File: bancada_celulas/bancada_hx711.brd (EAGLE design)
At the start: 124.4 x 102.5 mm, 17 parts

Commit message: KK connectors changed from 4mm to 2.54mm
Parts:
- X1, X11, X2, X3, X4, X5: value (none) -> 22-23-2041; device con-molex:KK-156-4 -> con-molex:22-23-2041
- X10, X6, X7, X8, X9: value (none) -> 22-23-2021; device con-molex:KK-156-2 -> con-molex:22-23-2021
- moved X10 6.35 mm to (91.4, 94.0)
- moved X9 5.08 mm to (67.3, 94.0)
- moved X8 5.08 mm to (19.1, 94.0)
- moved X6 5.08 mm to (115.6, 94.0)
- moved X4 3.81 mm to (88.9, 81.3)
- moved X5 2.54 mm to (113.0, 81.3)
- moved X1 2.54 mm to (16.5, 81.3)
- moved X3 2.54 mm to (64.8, 81.3)
- moved X7 2.54 mm to (43.2, 94.0)
- moved X2 1.27 mm to (40.6, 81.3)
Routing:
- net N$16: track 15.3 -> 12.7 mm
- net VCC: track 227.0 -> 229.1 mm
- net N$20: track 14.8 -> 12.7 mm
- net N$12: track 14.8 -> 12.7 mm
- net N$4: track 14.8 -> 12.7 mm
- net N$15: track 14.6 -> 12.7 mm
- net N$13: track 14.4 -> 12.7 mm
- net N$14: track 14.3 -> 12.7 mm
- net N$5: track 14.2 -> 12.7 mm
- net N$11: track 14.1 -> 12.7 mm
- net N$3: track 14.1 -> 12.7 mm
- net N$19: track 14.1 -> 12.7 mm
- net N$10: track 13.8 -> 12.7 mm
- net N$2: track 13.8 -> 12.7 mm
- net N$18: track 13.8 -> 12.7 mm
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
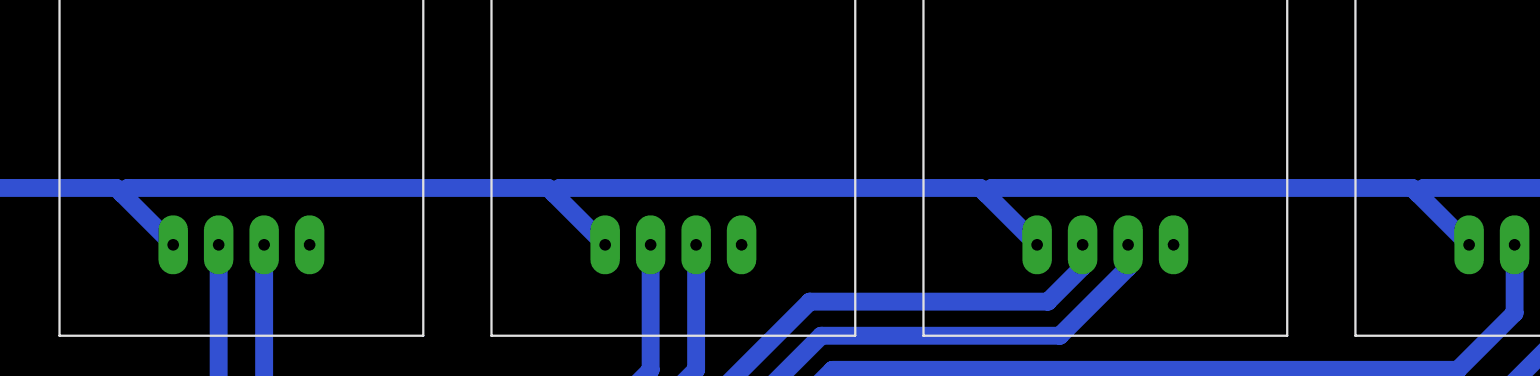
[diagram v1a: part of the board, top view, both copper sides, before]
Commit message: Increase the width of the grounded pins bridges and update DRC
The connections between the GND pins and the GND plane were too thin, so on the milling process they ended up not connected.

To solve this problem the width of those bridges were increased from 0.1016mm to 0.762mm changinf the GND polygon to 1.016mm width.

A new DRC was created as is used by both boards.
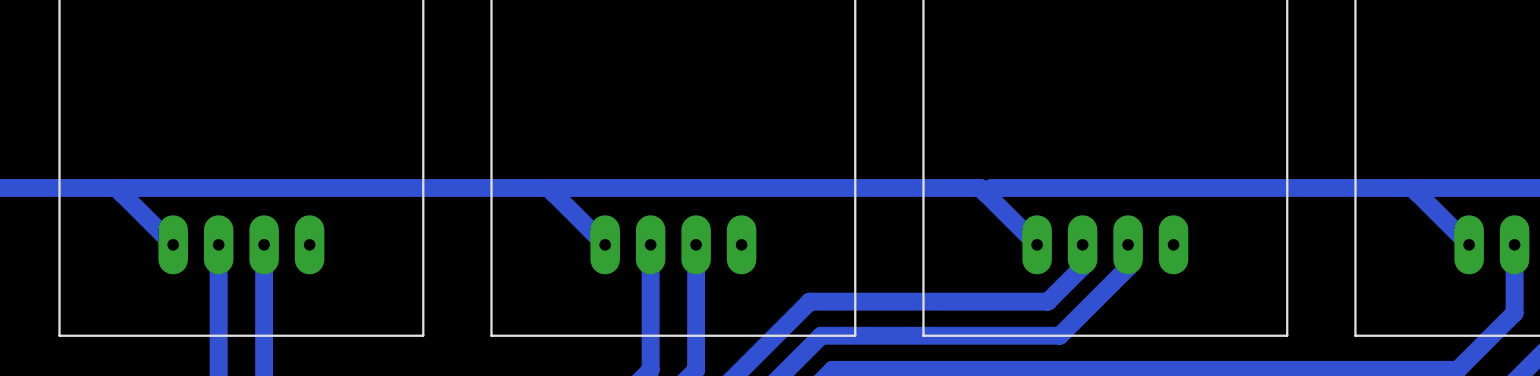
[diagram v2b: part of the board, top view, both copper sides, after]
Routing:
- net VCC: track 229.1 -> 231.0 mm
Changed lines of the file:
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@@
 <setting verticaltext="up"/>
 </settings>
-<grid distance="50" unitdist="mil" unit="mm" style="lines" multiple="1" display="no" altdistance="5" altunitdist="mil" altunit="mil"/>
+<grid distance="0.1" unitdist="mm" unit="mm" style="lines" multiple="1" display="no" altdistance="5" altunitdist="mil" altunit="mil"/>
 <layers>
 <layer number="1" name="Top" color="4" fill="1" visible="yes" active="yes"/>
@@
 </class>
 </classes>
-<designrules name="regraspcb2">
+<designrules name="drc_inep">
 <description language="de">&lt;b&gt;EAGLE Design Rules&lt;/b&gt;
 &lt;p&gt;
@@
 <param name="mtCopper" value="0.035mm 0.035mm 0.035mm 0.035mm 0.035mm 0.035mm 0.035mm 0.035mm 0.035mm 0.035mm 0.035mm 0.035mm 0.035mm 0.035mm 0.035mm 0.035mm"/>
 <param name="mtIsolate" value="1.5mm 0.15mm 0.2mm 0.15mm 0.2mm 0.15mm 0.2mm 0.15mm 0.2mm 0.15mm 0.2mm 0.15mm 0.2mm 0.15mm 0.2mm"/>
-<param name="mdWireWire" value="30mil"/>
-<param name="mdWirePad" value="30mil"/>
-<param name="mdWireVia" value="30mil"/>
-<param name="mdPadPad" value="30mil"/>
-<param name="mdPadVia" value="30mil"/>
-<param name="mdViaVia" value="30mil"/>
-<param name="mdSmdPad" value="30mil"/>
-<param name="mdSmdVia" value="30mil"/>
-<param name="mdSmdSmd" value="30mil"/>
+<param name="mdWireWire" value="20mil"/>
+<param name="mdWirePad" value="20mil"/>
+<param name="mdWireVia" value="20mil"/>
+<param name="mdPadPad" value="20mil"/>
+<param name="mdPadVia" value="20mil"/>
+<param name="mdViaVia" value="20mil"/>
+<param name="mdSmdPad" value="20mil"/>
+<param name="mdSmdVia" value="20mil"/>
+<param name="mdSmdSmd" value="20mil"/>
 <param name="mdViaViaSameLayer" value="8mil"/>
 <param name="mnLayersViaInSmd" value="2"/>
-<param name="mdCopperDimension" value="0.5mm"/>
+<param name="mdCopperDimension" value="1mm"/>
 <param name="mdDrill" value="1.5mm"/>
 <param name="mdSmdStop" value="0mil"/>
-<param name="msWidth" value="1mm"/>
-<param name="msDrill" value="1mm"/>
+<param name="msWidth" value="20mil"/>
+<param name="msDrill" value="0.2mm"/>
 <param name="msMicroVia" value="9.99mm"/>
 <param name="msBlindViaRatio" value="0.5"/>
@@
 <wire x1="103.505" y1="46.355" x2="103.8225" y2="46.0375" width="1" layer="16"/>
 <wire x1="103.8225" y1="46.0375" x2="106.68" y2="43.18" width="1" layer="16"/>
-<wire x1="80.01" y1="46.355" x2="103.505" y2="46.355" width="1" layer="16"/>
+<wire x1="80.01" y1="46.355" x2="102.87" y2="46.355" width="1" layer="16"/>
+<wire x1="102.87" y1="46.355" x2="103.505" y2="46.355" width="1" layer="16"/>
 <wire x1="80.01" y1="46.355" x2="79.6925" y2="46.0375" width="1" layer="16"/>
 <wire x1="29.845" y1="20.955" x2="62.23" y2="20.955" width="1" layer="16"/>
@@
 <wire x1="10.16" y1="45.085" x2="10.16" y2="43.18" width="1" layer="16"/>
 <wire x1="106.68" y1="26.67" x2="106.68" y2="24.13" width="1" layer="16"/>
+<wire x1="31.75" y1="46.355" x2="31.115" y2="46.355" width="1" layer="16"/>
+<wire x1="55.88" y1="46.355" x2="55.245" y2="46.355" width="1" layer="16"/>
+<wire x1="104.14" y1="46.355" x2="103.505" y2="46.355" width="1" layer="16"/>
 </signal>
 <signal name="GND">
@@
 <contactref element="X10" pad="2"/>
 <contactref element="X11" pad="3"/>
-<polygon width="0.1524" layer="16">
+<polygon width="0.762" layer="16">
 <vertex x="-5.08" y="106.68"/>
 <vertex x="128.27" y="106.68"/>

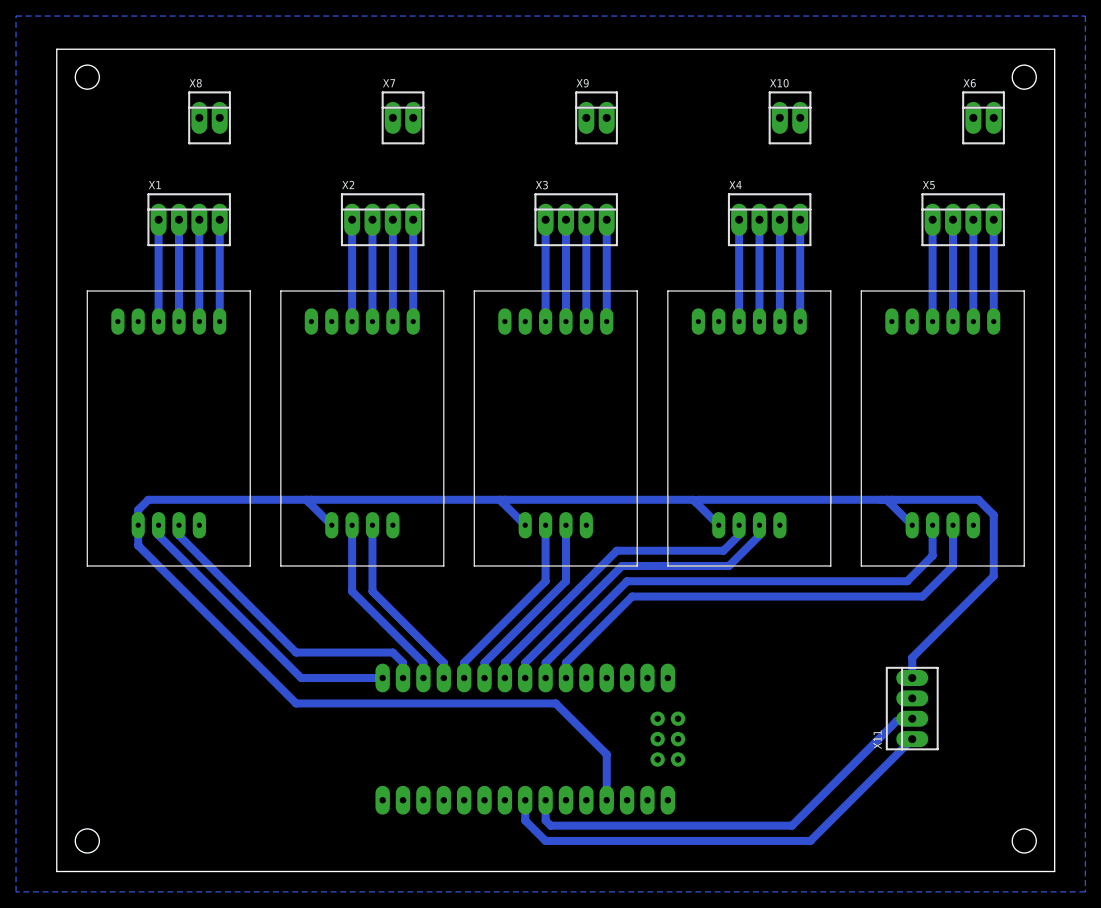
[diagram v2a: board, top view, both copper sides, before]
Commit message: Correct position for edge lines
Both top and right edge lines were bad positioned, in a way that the four board holes were not the same distance from the edges. This makes dificult to position them on CAD files for posterior case modeling.

Now the holes are 150mil apart from each edge.
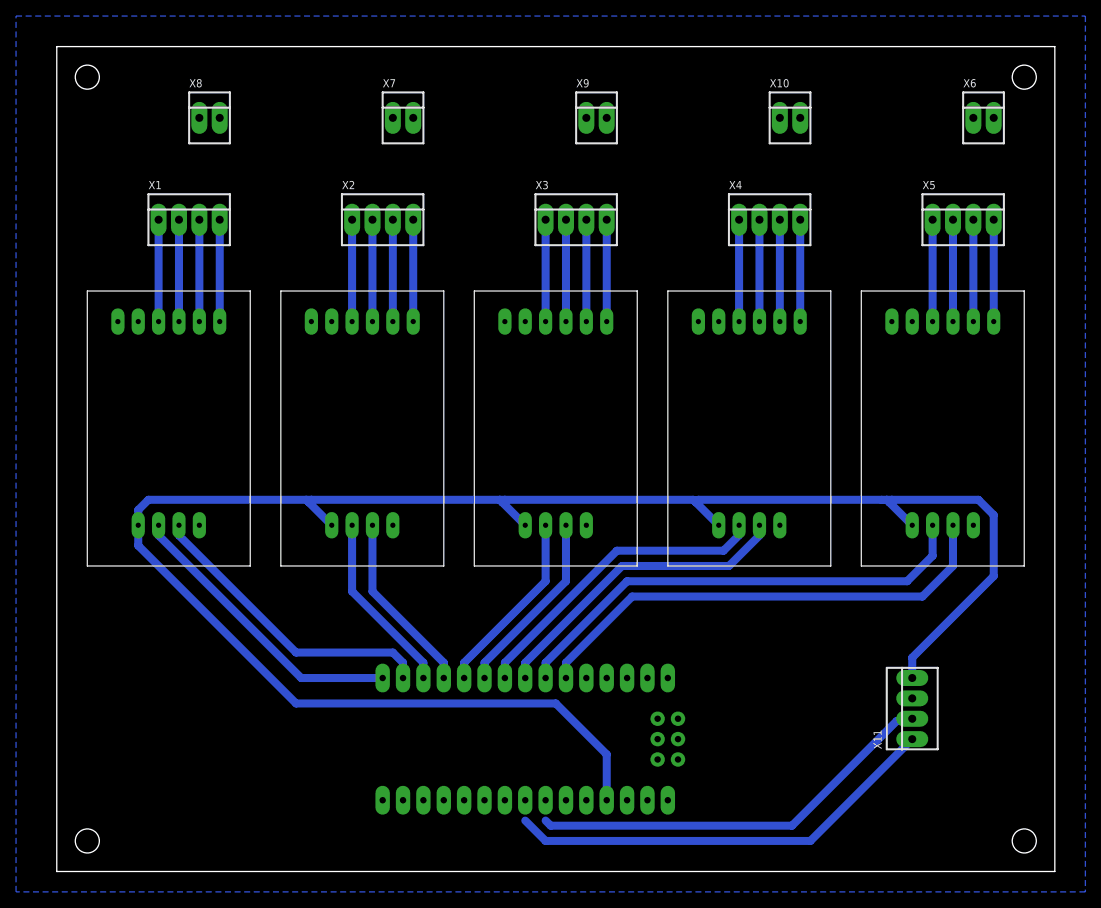
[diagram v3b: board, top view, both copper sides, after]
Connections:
- net N$21 renamed A5
- net N$22 renamed A4
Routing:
- net A4: track 57.1 -> 54.6 mm
- net A5: track 54.0 -> 51.5 mm
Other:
- board size 124.4 x 102.5 mm -> 124.5 x 102.9 mm
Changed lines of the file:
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@@
 <?xml version="1.0" encoding="utf-8"?>
 <!DOCTYPE eagle SYSTEM "eagle.dtd">
-<eagle version="8.6.0">
+<eagle version="9.0.0">
 <drawing>
 <settings>
@@
 <setting verticaltext="up"/>
 </settings>
-<grid distance="0.1" unitdist="mm" unit="mm" style="lines" multiple="1" display="no" altdistance="5" altunitdist="mil" altunit="mil"/>
+<grid distance="3.93700787" unitdist="mil" unit="inch" style="lines" multiple="1" display="no" altdistance="5" altunitdist="mil" altunit="mil"/>
 <layers>
 <layer number="1" name="Top" color="4" fill="1" visible="yes" active="yes"/>
@@
 <board>
 <plain>
-<wire x1="0" y1="0" x2="124.44" y2="0" width="0" layer="20"/>
-<wire x1="124.44" y1="0" x2="124.44" y2="102.54" width="0" layer="20"/>
-<wire x1="124.44" y1="102.54" x2="0" y2="102.54" width="0" layer="20"/>
-<wire x1="0" y1="102.54" x2="0" y2="0" width="0" layer="20"/>
+<wire x1="0" y1="0" x2="124.46" y2="0" width="0" layer="20"/>
+<wire x1="124.46" y1="0" x2="124.46" y2="102.87" width="0" layer="20"/>
+<wire x1="124.46" y1="102.87" x2="0" y2="102.87" width="0" layer="20"/>
+<wire x1="0" y1="102.87" x2="0" y2="0" width="0" layer="20"/>
 <hole x="3.81" y="3.81" drill="3"/>
 <hole x="120.65" y="3.81" drill="3"/>
@@
 <wire x1="109.22" y1="81.28" x2="109.22" y2="68.58" width="1" layer="16"/>
 </signal>
-<signal name="N$21">
+<signal name="A5">
 <contactref element="U$1" pad="A5"/>
 <contactref element="X11" pad="2"/>
-<wire x1="60.96" y1="8.89" x2="60.96" y2="6.35" width="1" layer="16"/>
 <wire x1="61.595" y1="5.715" x2="60.96" y2="6.35" width="1" layer="16"/>
 <wire x1="106.68" y1="19.05" x2="106.402" y2="18.772" width="1" layer="16"/>
@@
 <wire x1="104.74304375" y1="18.772" x2="91.68604375" y2="5.715" width="1" layer="16"/>
 <wire x1="91.68604375" y1="5.715" x2="61.595" y2="5.715" width="1" layer="16"/>
-</signal>
-<signal name="N$22">
+<wire x1="60.96" y1="6.35" x2="60.96" y2="8.89" width="0" layer="19" extent="16-16"/>
+</signal>
+<signal name="A4">
 <contactref element="U$1" pad="A4"/>
 <contactref element="X11" pad="1"/>
-<wire x1="58.42" y1="8.89" x2="58.42" y2="6.35" width="1" layer="16"/>
 <wire x1="60.96" y1="3.81" x2="58.42" y2="6.35" width="1" layer="16"/>
 <wire x1="106.68" y1="16.51" x2="93.98" y2="3.81" width="1" layer="16"/>
 <wire x1="93.98" y1="3.81" x2="60.96" y2="3.81" width="1" layer="16"/>
+<wire x1="58.42" y1="6.35" x2="58.42" y2="8.89" width="0" layer="19" extent="16-16"/>
 </signal>
 </signals>

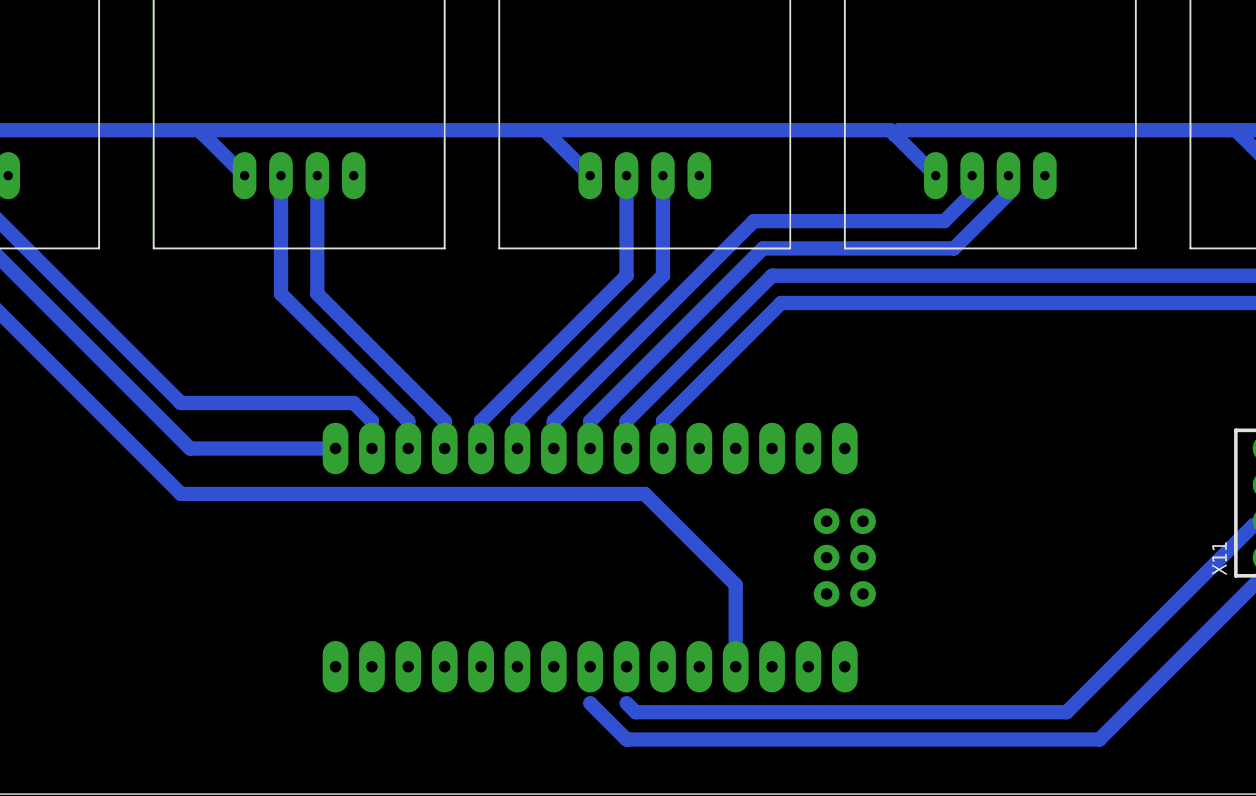
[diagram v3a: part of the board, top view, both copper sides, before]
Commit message: Add jumpers (or 0ohm resistors)
In previous design, some ground planes were unconnected to each other. It was meant to be added jumper wires after production.

This commit changes this to actual jumpers, with pins, so they don't need to be soldered from bottom, but can actually be placed on top, like any other through-hole component. 0ohm through-hole resistors can also be used.
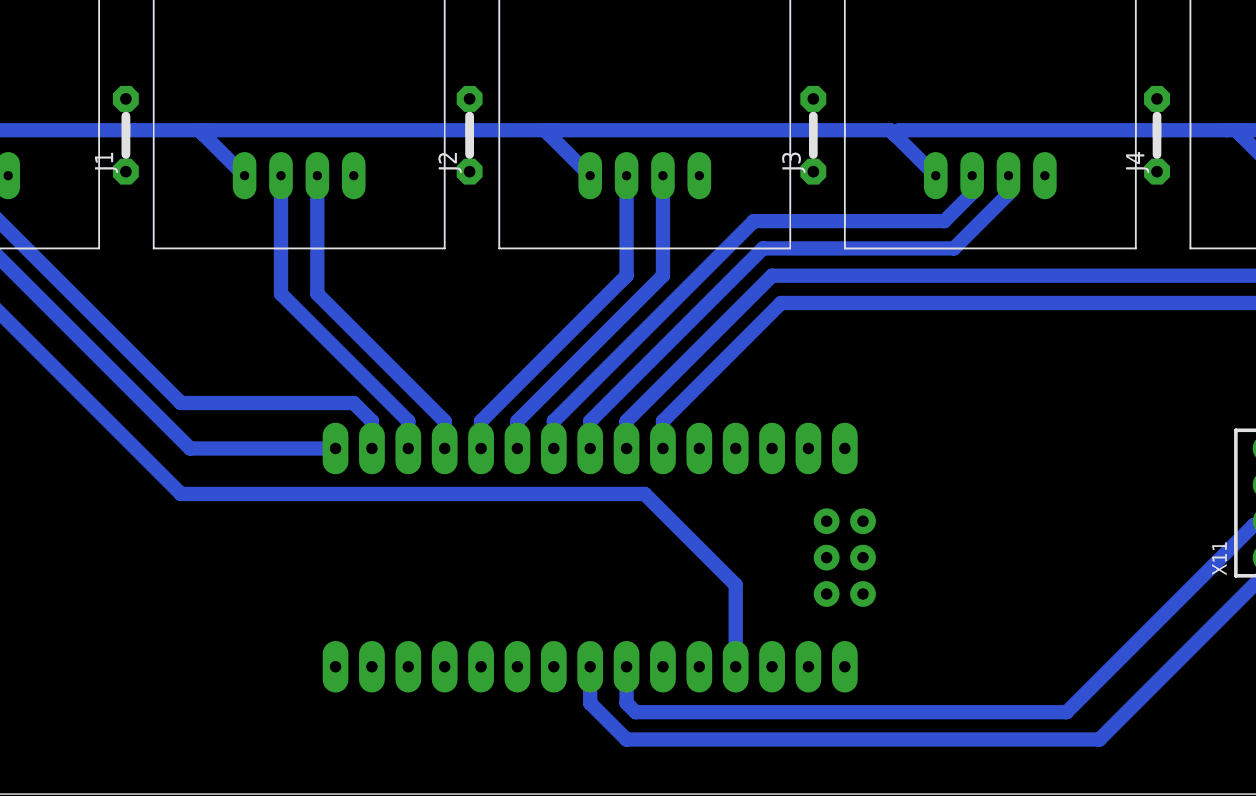
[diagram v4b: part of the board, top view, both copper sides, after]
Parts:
- added J1, J2, J3, J4: J5MM, jumper:05
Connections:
- net GND: now also J1.1, J1.2, J2.1, J2.2, J3.1, J3.2, J4.1, J4.2
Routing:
- net A5: track 51.5 -> 54.0 mm
- net A4: track 54.6 -> 57.1 mm
